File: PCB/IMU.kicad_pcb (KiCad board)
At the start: 2 copper layers, 65 parts, among them IC1 STM32F405VGT, IC2 ADP3335ARMZ-3.3, IC3 ADP3335ARMZ-5, IC4 MS5611-01BA03, P1 UART1, P2 SWD, P3 UART2, P4 SPI, P5 BATTERY, P6 3V3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

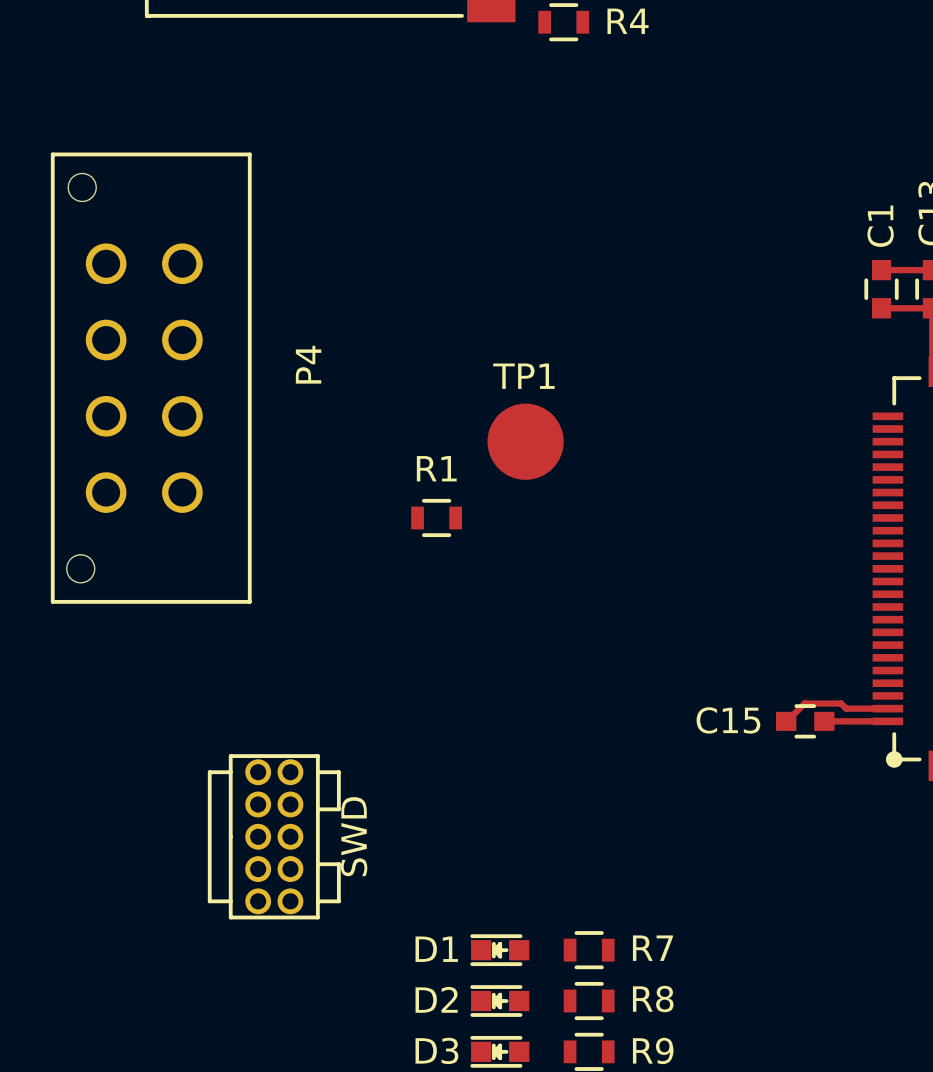
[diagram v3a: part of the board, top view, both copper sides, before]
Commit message: PCB: re-assign SD_CARD_DETECT signal to better side of STM32
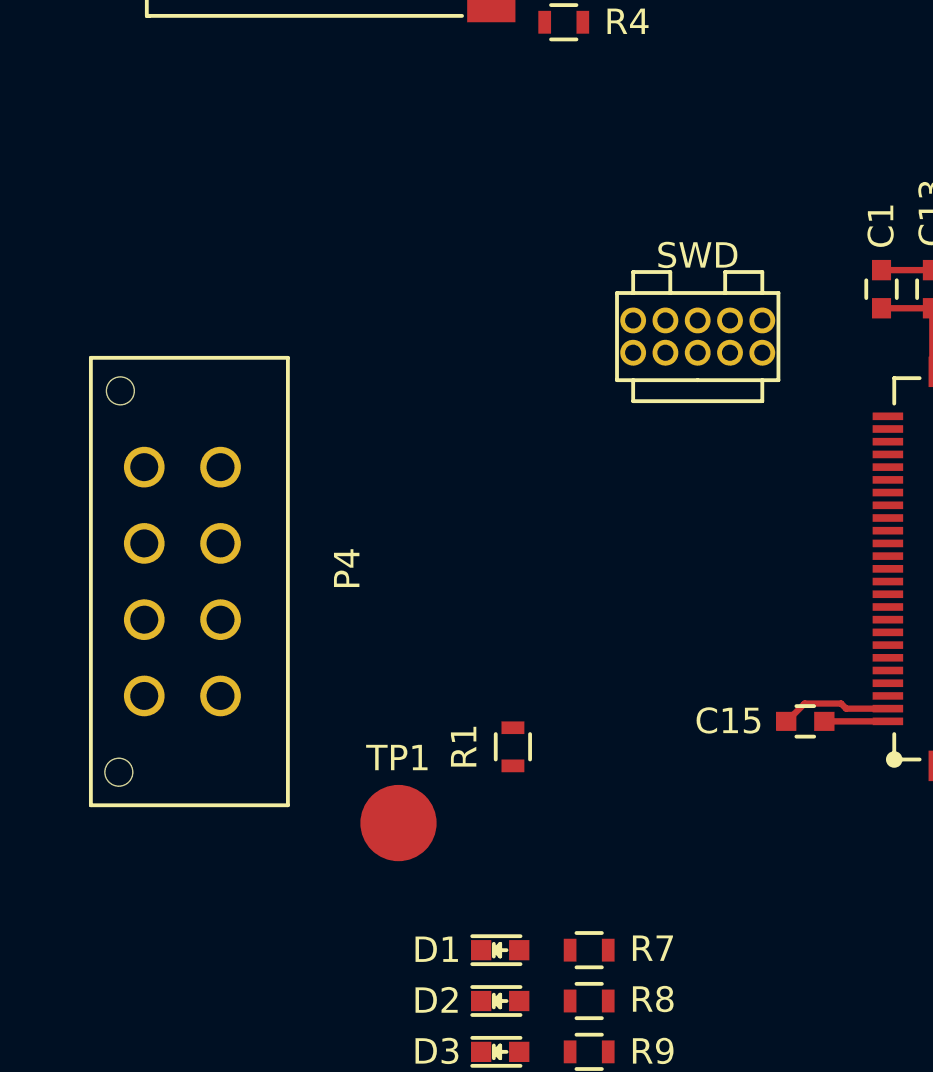
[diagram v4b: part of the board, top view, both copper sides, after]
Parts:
- moved P2 29.3 mm to (168.8, 94.5), turned to 180 degrees
- moved TP1 15.8 mm to (154.5, 113.0)
- moved R1 9.49 mm to (159.0, 110.0), turned to 90 degrees
- moved P4 8.14 mm to (147.5, 99.0)
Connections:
- IC1 pad 5: /SDCard/CARD_DETECT -> Net-(IC1-Pad5)
- IC1 pad 84: Net-(IC1-Pad84) -> /SDCard/CARD_DETECT

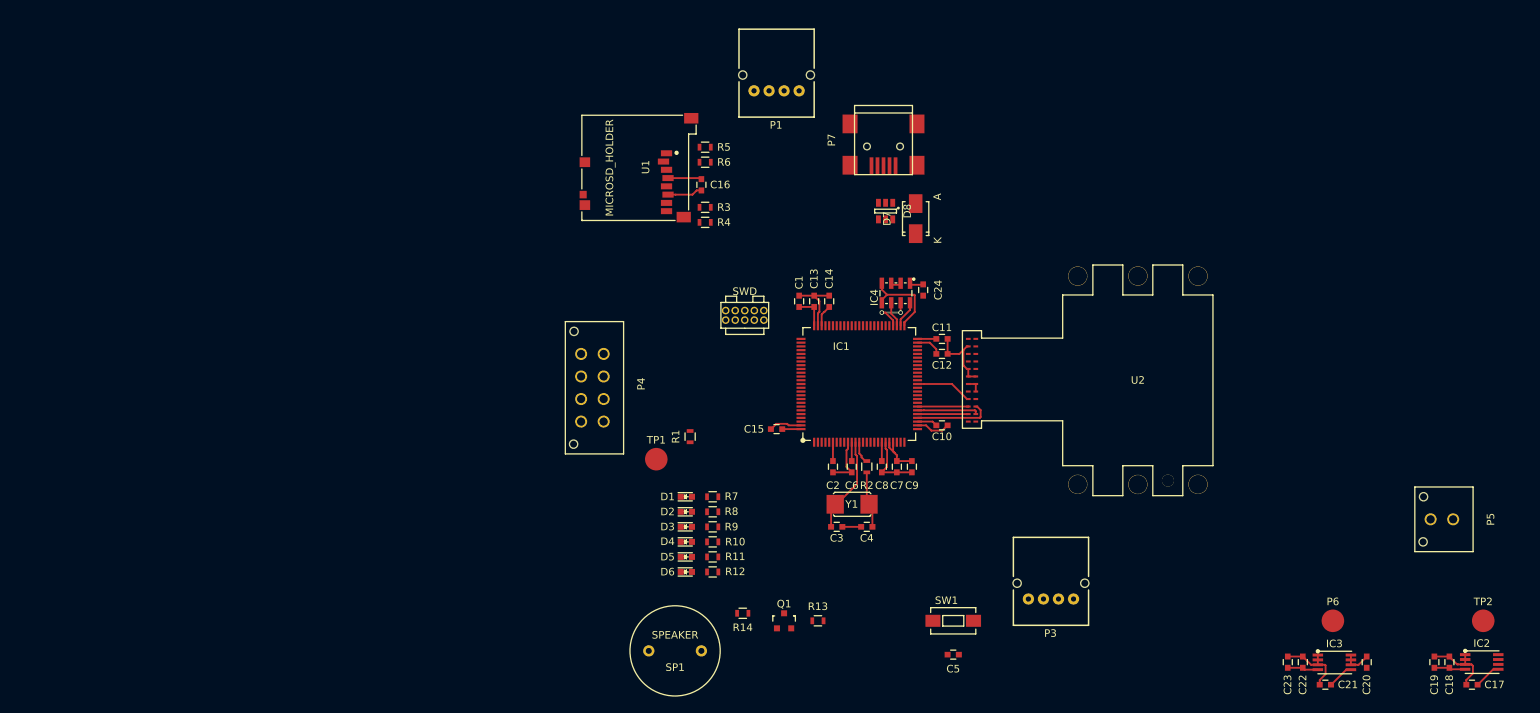
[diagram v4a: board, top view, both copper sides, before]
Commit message: PCB: shuffle footprint and route some more uncontroversial tracks
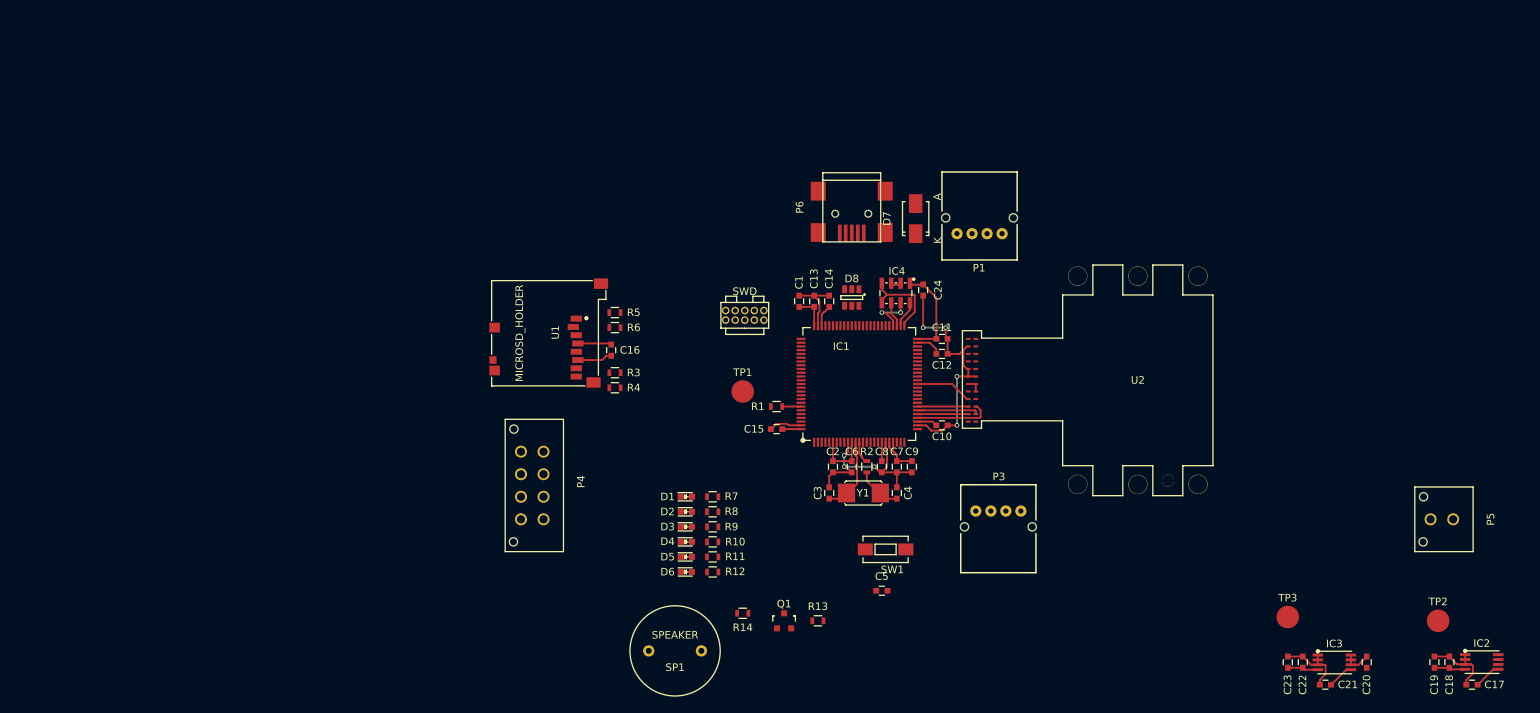
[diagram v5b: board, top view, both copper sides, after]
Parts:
- moved P1 33.0 mm to (194.5, 83.0)
- moved TP3 26.0 mm to (238.5, 134.0)
- moved C16 25.1 mm to (148.5, 98.5)
- moved R3 25.1 mm to (149.0, 101.5)
- moved R4 25.1 mm to (149.0, 103.5)
- moved R5 25.1 mm to (149.0, 93.5)
- moved R6 25.1 mm to (149.0, 95.5)
- moved U1 25.1 mm to (132.6, 103.2)
- moved P4 15.3 mm to (139.5, 112.0)
- moved TP1 14.6 mm to (166.0, 104.0)
- moved TP2 14.0 mm to (258.5, 134.5)
- moved SW1 13.1 mm to (185.0, 125.0), turned to 180 degrees
- moved C5 12.7 mm to (184.5, 130.5), turned to 0 degrees
- moved D8 12.3 mm to (180.5, 91.5)
- moved R1 12.2 mm to (170.5, 106.0), turned to 0 degrees
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- renumbered P7 to P6, P6 to TP2, TP2 to TP3
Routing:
- net GND: track 59.3 -> 84.9 mm, vias 0 -> 7
- net +3V3: track 42.3 -> 52.8 mm
- net Net-(C3-Pad1): track 12.8 -> 10.1 mm
- net /BOOT0: track 0.00 -> 2.50 mm
- net Net-(C4-Pad1): track 7.56 -> 6.26 mm

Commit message: PCB: double-check the UART connector wiring
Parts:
- moved P1 8.73 mm to (198.0, 91.0)
- moved P3 5.98 mm to (204.0, 114.0)
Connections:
- P1 pad 2: USART1_TX -> USART1_RX
- P1 pad 3: USART1_RX -> USART1_TX
- P3 pad 2: USART2_TX -> USART2_RX
- P3 pad 3: USART2_RX -> USART2_TX
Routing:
- net GND: track 84.9 -> 80.6 mm
- net +3V3: track 52.8 -> 48.5 mm
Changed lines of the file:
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@@
     (thickness 1.6)
     (drawings 0)
-    (tracks 202)
+    (tracks 199)
     (zones 0)
     (modules 65)
@@
   )
   (module IMU:S04B-PASK-2 (layer F.Cu)
-    (at 194.5 83)
+    (at 198 91)
     (fp_text reference P1 (at 2.93 4.57) (layer F.SilkS)
       (effects (font (size 1 1) (thickness 0.15)))
@@
       (net 1 +3V3))
     (pad 2 thru_hole circle (at 2 0) (size 1.5 1.5) (drill 0.7) (layers *.Cu *.Mask F.SilkS)
+      (net 78 USART1_RX))
+    (pad 3 thru_hole circle (at 4 0) (size 1.5 1.5) (drill 0.7) (layers *.Cu *.Mask F.SilkS)
       (net 77 USART1_TX))
-    (pad 3 thru_hole circle (at 4 0) (size 1.5 1.5) (drill 0.7) (layers *.Cu *.Mask F.SilkS)
-      (net 78 USART1_RX))
     (pad 4 thru_hole circle (at 6 0) (size 1.5 1.5) (drill 0.7) (layers *.Cu *.Mask F.SilkS)
       (net 2 GND))
@@
   )
   (module IMU:S04B-PASK-2 (layer F.Cu)
-    (at 203 119.9 180)
-    (fp_text reference P3 (at 2.93 4.57 180) (layer F.SilkS)
+    (at 204 114 180)
+    (fp_text reference P3 (at -3.5 2 180) (layer F.SilkS)
       (effects (font (size 1 1) (thickness 0.15)))
     )
@@
       (net 1 +3V3))
     (pad 2 thru_hole circle (at 2 0 180) (size 1.5 1.5) (drill 0.7) (layers *.Cu *.Mask F.SilkS)
+      (net 39 USART2_RX))
+    (pad 3 thru_hole circle (at 4 0 180) (size 1.5 1.5) (drill 0.7) (layers *.Cu *.Mask F.SilkS)
       (net 38 USART2_TX))
-    (pad 3 thru_hole circle (at 4 0 180) (size 1.5 1.5) (drill 0.7) (layers *.Cu *.Mask F.SilkS)
-      (net 39 USART2_RX))
     (pad 4 thru_hole circle (at 6 0 180) (size 1.5 1.5) (drill 0.7) (layers *.Cu *.Mask F.SilkS)
       (net 2 GND))
@@
       (net 82 SDIO_D2))
   )
+  (module IMU:XTAL50x32 (layer F.Cu)
+    (at 180 117.5)
+    (fp_text reference Y1 (at 2 0) (layer F.SilkS)
+      (effects (font (size 1 1) (thickness 0.15)))
+    )
+    (fp_text value 8M (at 2.5 2.6) (layer F.SilkS) hide
+      (effects (font (size 1 1) (thickness 0.15)))
+    )
+    (fp_line (start -0.25 -1.6) (end 4.35 -1.6) (layer F.SilkS) (width 0.15))
+    (fp_line (start 4.55 -1.4) (end 4.35 -1.6) (layer F.SilkS) (width 0.15))
+    (fp_line (start -0.45 -1.4) (end -0.25 -1.6) (layer F.SilkS) (width 0.15))
+    (fp_line (start -0.3 1.6) (end 4.4 1.6) (layer F.SilkS) (width 0.15))
+    (fp_line (start -0.45 1.4) (end -0.3 1.6) (layer F.SilkS) (width 0.15))
+    (fp_line (start 4.55 1.4) (end 4.4 1.6) (layer F.SilkS) (width 0.15))
+    (pad 1 smd rect (at 0 0) (size 2.3 2.5) (drill (offset -0.2 0)) (layers F.Cu F.Paste F.Mask)
+      (net 3 "Net-(C3-Pad1)"))
+    (pad 2 smd rect (at 4.1 0) (size 2.3 2.5) (drill (offset 0.2 0)) (layers F.Cu F.Paste F.Mask)
+      (net 4 "Net-(C4-Pad1)"))
+  )
   (module IMU:ADIS16405BMLZ (layer F.Cu)
     (at 241.119798 97.000022 180)
@@
       (effects (font (size 1 1) (thickness 0.15)))
     )
-    (fp_text user "Copyright 2015 Accelerated Designs. All rights reserved." (at 0 0 180) (layer F.SilkS) hide
+    (fp_text user "Copyright 2015 Accelerated Designs. All rights reserved." (at 21.5 -9 180) (layer F.SilkS) hide
       (effects (font (size 0.127 0.127) (thickness 0.002)))
     )
@@
     (pad 32 thru_hole circle (at 22.559899 -19.362802 180) (size 2.5654 2.5654) (drill 2.4892) (layers *.Cu *.Mask F.SilkS))
   )
-  (module IMU:XTAL50x32 (layer F.Cu)
-    (at 180 117.5)
-    (fp_text reference Y1 (at 2 0) (layer F.SilkS)
-      (effects (font (size 1 1) (thickness 0.15)))
-    )
-    (fp_text value 8M (at 2.5 2.6) (layer F.SilkS) hide
-      (effects (font (size 1 1) (thickness 0.15)))
-    )
-    (fp_line (start -0.25 -1.6) (end 4.35 -1.6) (layer F.SilkS) (width 0.15))
-    (fp_line (start 4.55 -1.4) (end 4.35 -1.6) (layer F.SilkS) (width 0.15))
-    (fp_line (start -0.45 -1.4) (end -0.25 -1.6) (layer F.SilkS) (width 0.15))
-    (fp_line (start -0.3 1.6) (end 4.4 1.6) (layer F.SilkS) (width 0.15))
-    (fp_line (start -0.45 1.4) (end -0.3 1.6) (layer F.SilkS) (width 0.15))
-    (fp_line (start 4.55 1.4) (end 4.4 1.6) (layer F.SilkS) (width 0.15))
-    (pad 1 smd rect (at 0 0) (size 2.3 2.5) (drill (offset -0.2 0)) (layers F.Cu F.Paste F.Mask)
-      (net 3 "Net-(C3-Pad1)"))
-    (pad 2 smd rect (at 4.1 0) (size 2.3 2.5) (drill (offset 0.2 0)) (layers F.Cu F.Paste F.Mask)
-      (net 4 "Net-(C4-Pad1)"))
-  )
   (segment (start 178 113.25) (end 180.5 113.25) (width 0.25) (layer F.Cu) (net 1))
   (segment (start 190 89.75) (end 190 89.775) (width 0.25) (layer F.Cu) (net 1))
@@
   (segment (start 189.25 108) (end 191.25 108) (width 0.25) (layer F.Cu) (net 1))
   (segment (start 191.25 108) (end 191.75 108.5) (width 0.25) (layer F.Cu) (net 1))
-  (segment (start 144.06 97.61) (end 148.36 97.61) (width 0.25) (layer F.Cu) (net 1))
   (segment (start 148.36 97.61) (end 148.5 97.75) (width 0.25) (layer F.Cu) (net 1))
   (segment (start 262.1 140.3) (end 262.935002 140.3) (width 0.25) (layer F.Cu) (net 1))
@@
   (segment (start 173.75 109) (end 171.25 109) (width 0.25) (layer F.Cu) (net 1))
   (segment (start 175.5 92.75) (end 173.5 92.75) (width 0.25) (layer F.Cu) (net 1))
+  (segment (start 191.75 114.75) (end 192 114.5) (width 0.25) (layer F.Cu) (net 2))
   (segment (start 183.5 114) (end 179.5 114) (width 0.25) (layer B.Cu) (net 2))
   (segment (start 184.5 114.75) (end 184.25 114.75) (width 0.25) (layer F.Cu) (net 2))
@@
   (segment (start 196 102.000012) (end 196 101.000014) (width 0.25) (layer F.Cu) (net 2))
   (segment (start 196 102.000012) (end 196.999998 102.000012) (width 0.25) (layer F.Cu) (net 2))
-  (segment (start 148.5 99.25) (end 147.875 99.25) (width 0.25) (layer F.Cu) (net 2))
-  (segment (start 147.875 99.25) (end 147.315 99.81) (width 0.25) (layer F.Cu) (net 2))
-  (segment (start 147.315 99.81) (end 145.06 99.81) (width 0.25) (layer F.Cu) (net 2))
-  (segment (start 145.06 99.81) (end 144.06 99.81) (width 0.25) (layer F.Cu) (net 2))
   (segment (start 240.5 140.75) (end 238.5 140.75) (width 0.25) (layer F.Cu) (net 2))
   (segment (start 240.5 140.75) (end 240.75 141) (width 0.25) (layer F.Cu) (net 2))
@@
   (segment (start 181.8 112.75) (end 182.3 113.25) (width 0.25) (layer F.Cu) (net 31))
   (segment (start 182.3 113.25) (end 182.5 113.25) (width 0.25) (layer F.Cu) (net 31))
+  (segment (start 189.25 109) (end 189.7 109) (width 0.25) (layer F.Cu) (net 39))
   (segment (start 189.25 107.5) (end 197.542202 107.5) (width 0.25) (layer F.Cu) (net 40))
   (segment (start 197.542202 107.5) (end 197.642499 107.399703) (width 0.25) (layer F.Cu) (net 40))
